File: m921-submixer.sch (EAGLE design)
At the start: 65 parts, among them U1 SCREW-M2X8, U10 FX2-20P-1.27DS, U11 ERM1-5MM, U2 SCREW-M2X8, U3 NUT-M2-SELFLOCK, U4 NUT-M2-SELFLOCK, U5 FX2-20S-1.27DS, U6 SCREW-M2X8, U7 SCREW-M2X8, U8 NUT-M2-SELFLOCK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

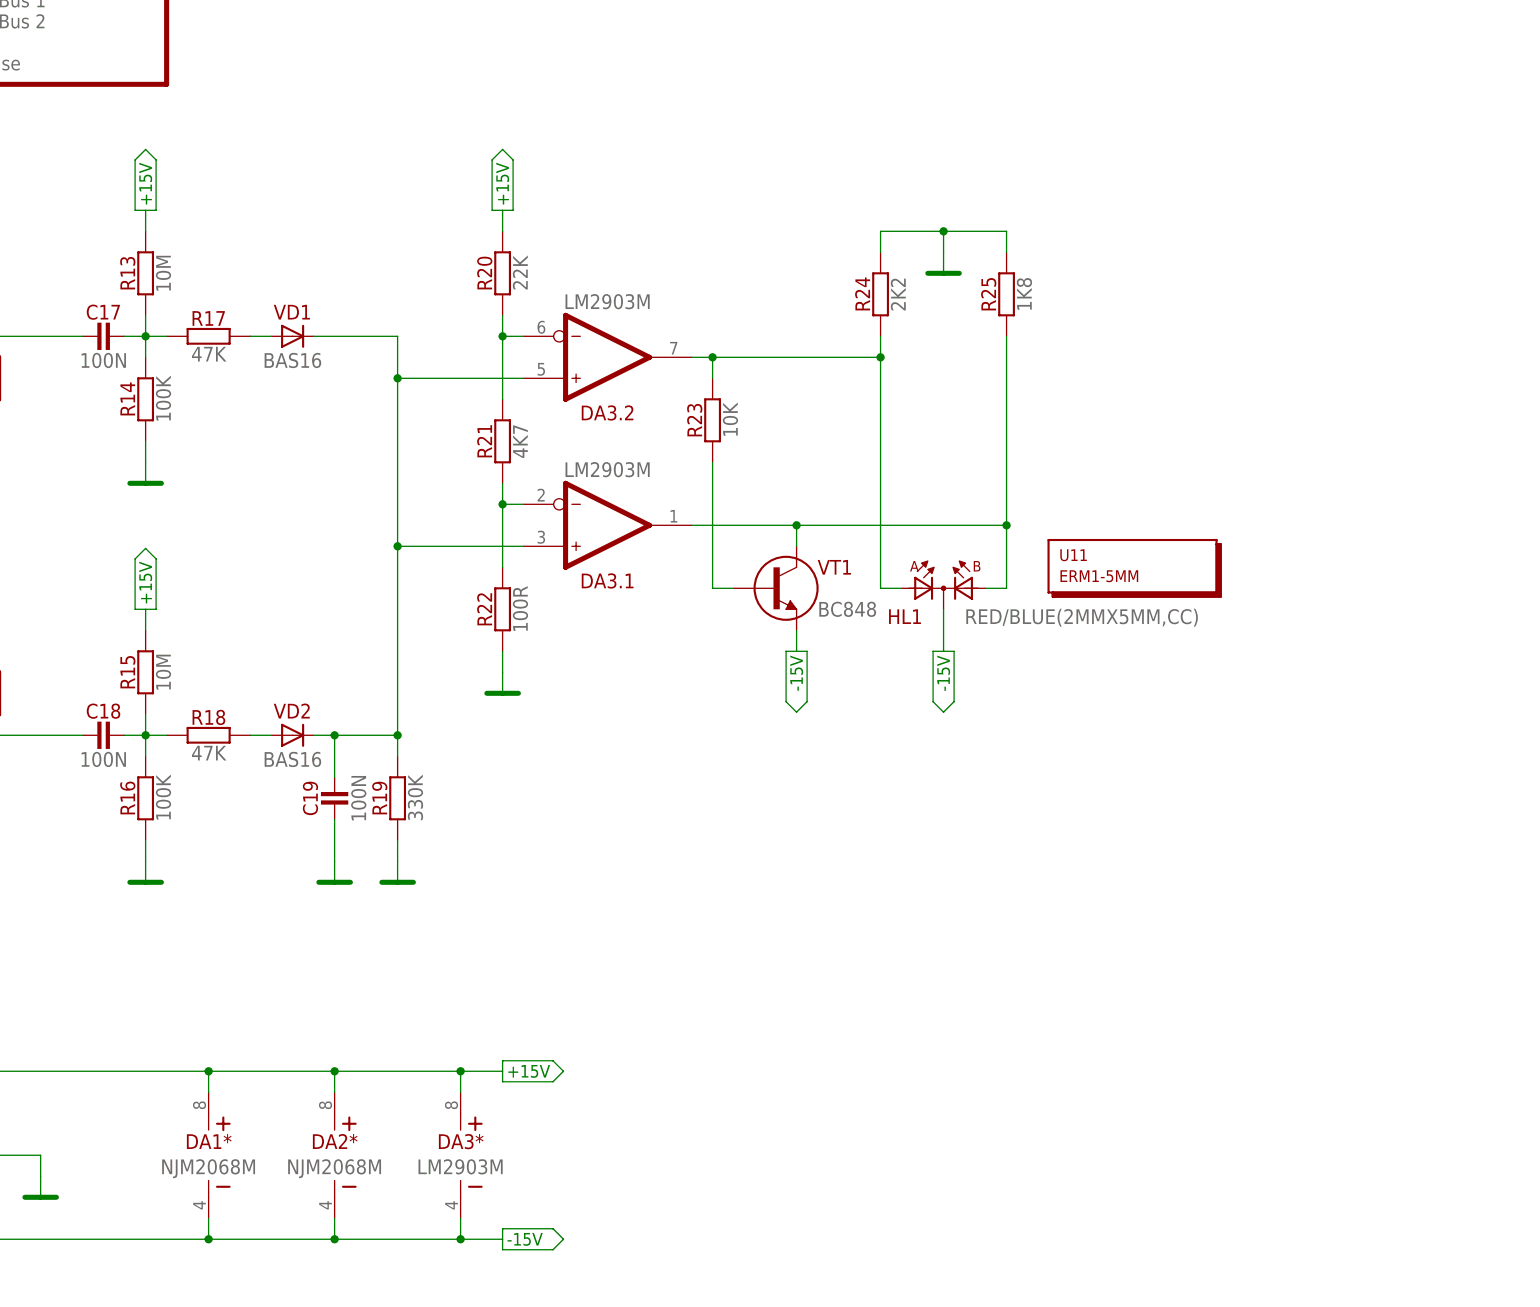
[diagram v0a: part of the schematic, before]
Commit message: M921 Updated signal indicator
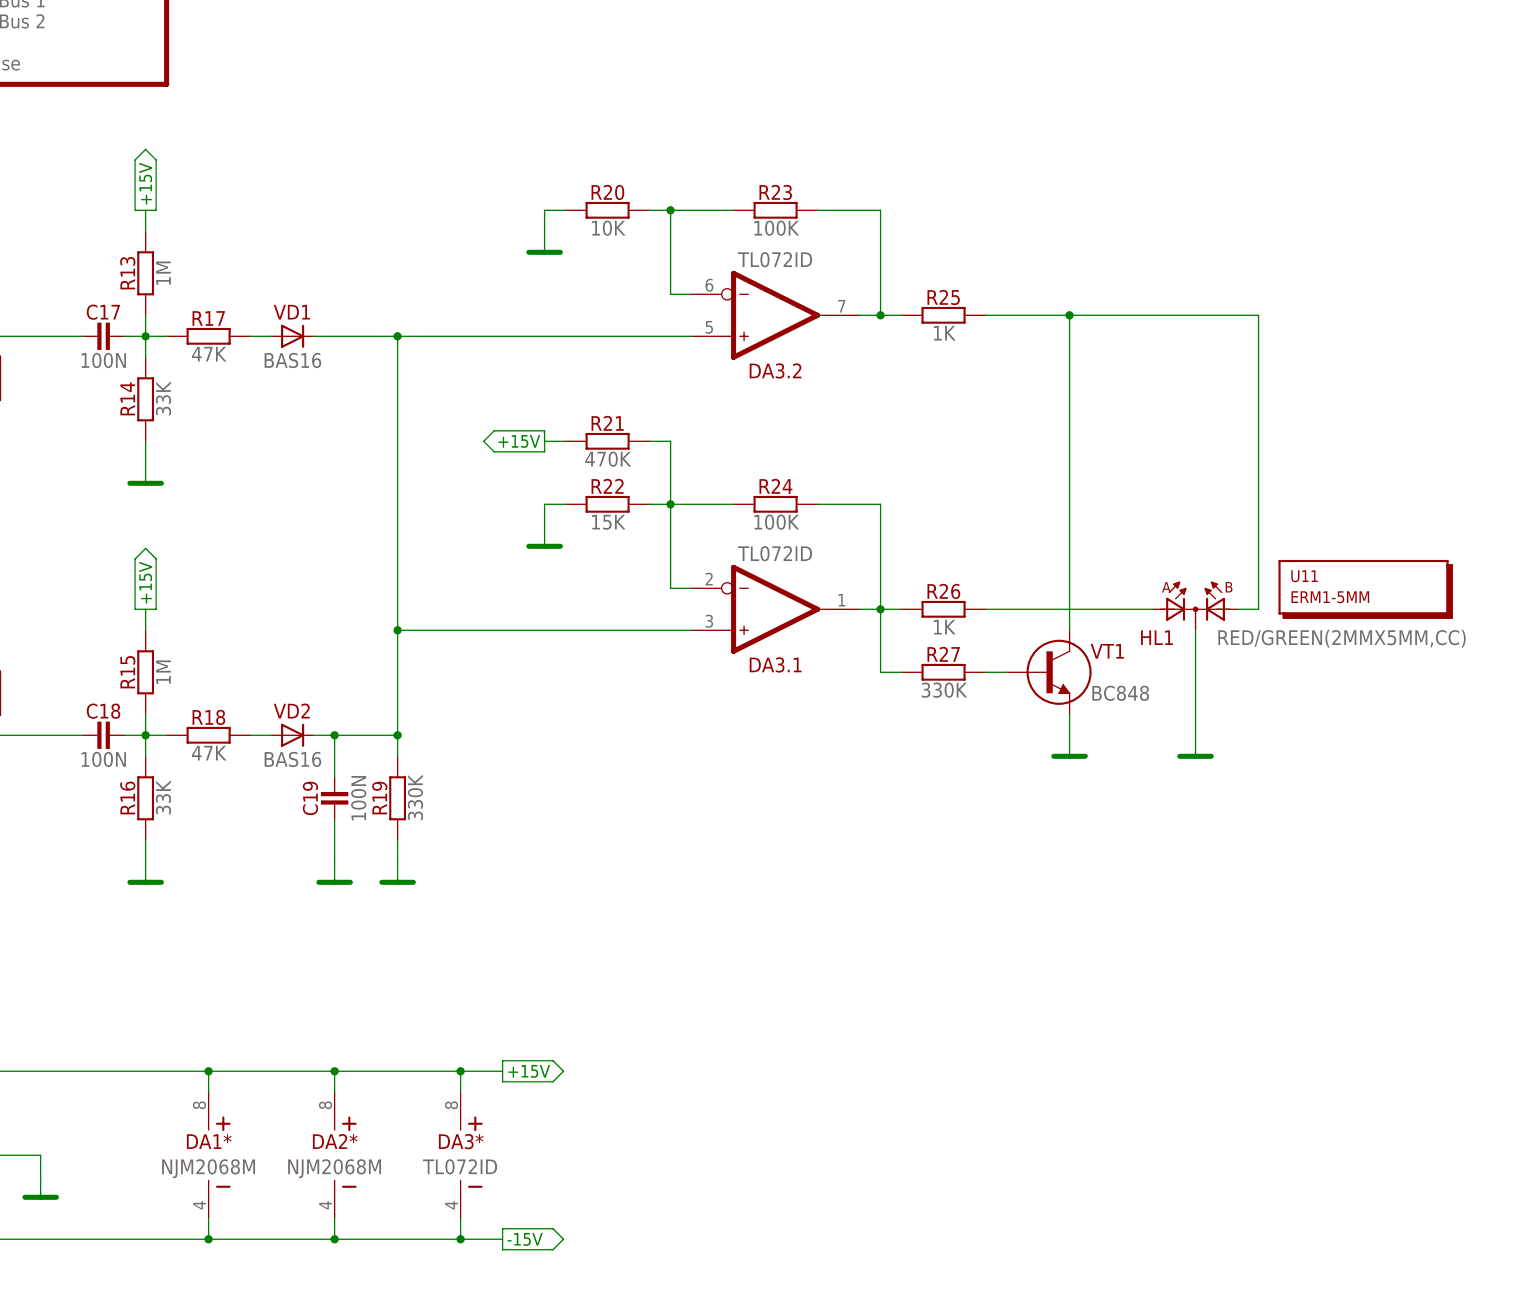
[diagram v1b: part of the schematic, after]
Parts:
- added R26: 1K, resistors:1K
- added R27: 330K, resistors:330K
- DA3: value LM2903M -> TL072ID; device ic-fairchild:LM2903M -> ic-ti:TL072ID
- HL1: value RED/BLUE(2MMX5MM,CC) -> RED/GREEN(2MMX5MM,CC); device optoelectronics:RED/BLUE(2MMX5MM,CC) -> optoelectronics:RED/GREEN(2MMX5MM,CC)
- R13, R15: value 10M -> 1M; device resistors:10M -> resistors:1M
- R14, R16: value 100K -> 33K; device resistors:100K -> resistors:33K
- R20: value 22K -> 10K; device resistors:22K -> resistors:10K
- R21: value 4K7 -> 470K; device resistors:4K7 -> resistors:470K
- R22: value 100R -> 15K; device resistors:100R -> resistors:15K
- R23: value 10K -> 100K; device resistors:10K -> resistors:100K
- R24: value 2K2 -> 100K; device resistors:2K2 -> resistors:100K
- R25: value 1K8 -> 1K; device resistors:1K8 -> resistors:1K
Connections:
- removed net N$23 (its old number): DA3.1.IN-, R21.1, R22.2
- removed net N$25: DA3.1.OUT, HL1.A2, R25.1, VT1.C
- removed net N$47: DA3.2.IN-, R20.1, R21.2
- removed net N$48: DA3.2.OUT, HL1.A1, R23.2, R24.1
- removed net N$49: R23.1, VT1.B
- new net N$13: DA3.2.IN-, R20.2, R23.1
- new net N$17: DA3.2.OUT, R23.2, R25.1
- new net N$29: HL1.A2, R25.2, VT1.C
- new net N$30: DA3.1.IN-, R21.2, R22.2, R24.1
- new net N$31: DA3.1.OUT, R24.2, R26.1, R27.1
- new net N$32: R27.2, VT1.B
- new net N$33: HL1.A1, R26.2
- net +15V: now also R21.1; no longer R20.2
- net -15V: no longer HL1.K, VT1.E
- net GND: now also HL1.K, R20.1, VT1.E; no longer R24.2, R25.2
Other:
- moved on the sheet: DA3.1, DA3.2, HL1, R20, R21, R22, R23, R24, R25, U11, VT1
